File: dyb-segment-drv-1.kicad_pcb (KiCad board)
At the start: 2 copper layers, 76 x 76 mm, 192 parts, among them J1 Conn_01x10, Q1 HL2300, Q10 HL2300, Q11 HL2300, Q12 HL2300, Q13 HL2300, Q14 HL2300, Q15 HL2300, Q16 HL2300, Q2 HL2300, Q3 HL2300, Q4 HL2300, Q5 HL2300, Q6 HL2300, Q7 HL2300, Q8 HL2300, Q9 HL2300, SW1 SW_SPDT, U1 AP2112K-1.8, U10 74AUC2G32, U11 74AUC2G32, U12 74AUC2G32, U13 74AUC2G32, U14 74AUC2G32, U15 Inverter_Schmitt_Dual, U16 Inverter_Schmitt_Dual, U17 SN74AUP2G08, U18 SN74AUP2G08, U19 SN74AUP2G08, U2 GS3911AG, U20 SN74AUP2G08, U21 SN74AUP2G08, U22 74AUC2G32, U23 74AUC2G32, U24 74AUC2G32, U25 74AUC2G32, U26 74AUC2G32, U27 GS3911AG, U28 SN74AUP2G08, U29 SN74AUP2G08, U3 SN74AUP2G08, U30 SN74AUP2G08, U31 SN74AUP2G08, U32 SN74AUP2G08, U33 SN74AUP2G08, U34 74AUC2G32, U35 74AUC2G32, U36 74AUC2G32, U37 74AUC2G32, U38 74AUC2G32, U39 74AUC2G32, U4 SN74AUP2G08, U40 Inverter_Schmitt_Dual, U41 Inverter_Schmitt_Dual, U42 SN74AUP2G08, U43 SN74AUP2G08, U44 SN74AUP2G08, U45 SN74AUP2G08, U46 SN74AUP2G08, U47 74AUC2G32, U48 74AUC2G32, U49 74AUC2G32, U5 SN74AUP2G08, U50 74AUC2G32, U51 74AUC2G32, U6 SN74AUP2G08, U7 SN74AUP2G08, U8 SN74AUP2G08, U9 74AUC2G32

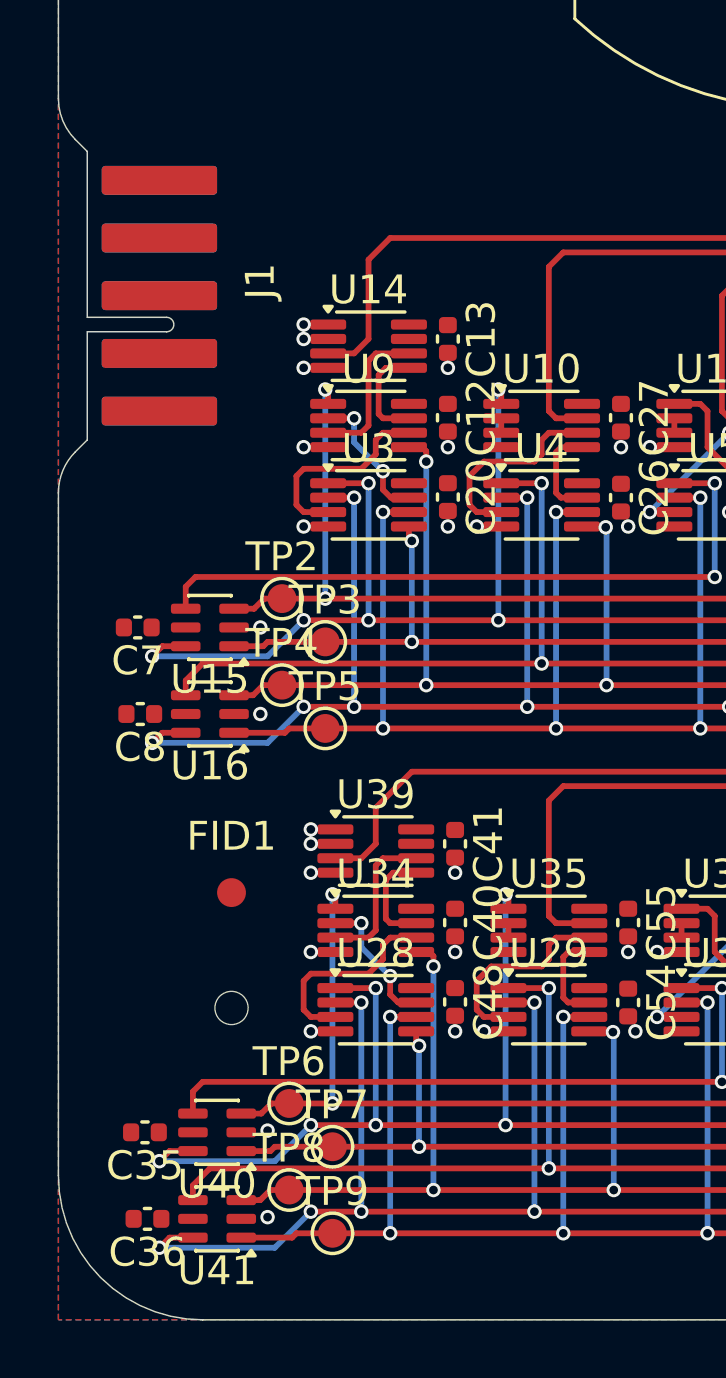
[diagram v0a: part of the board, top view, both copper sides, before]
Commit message: pcb: route gates inputs
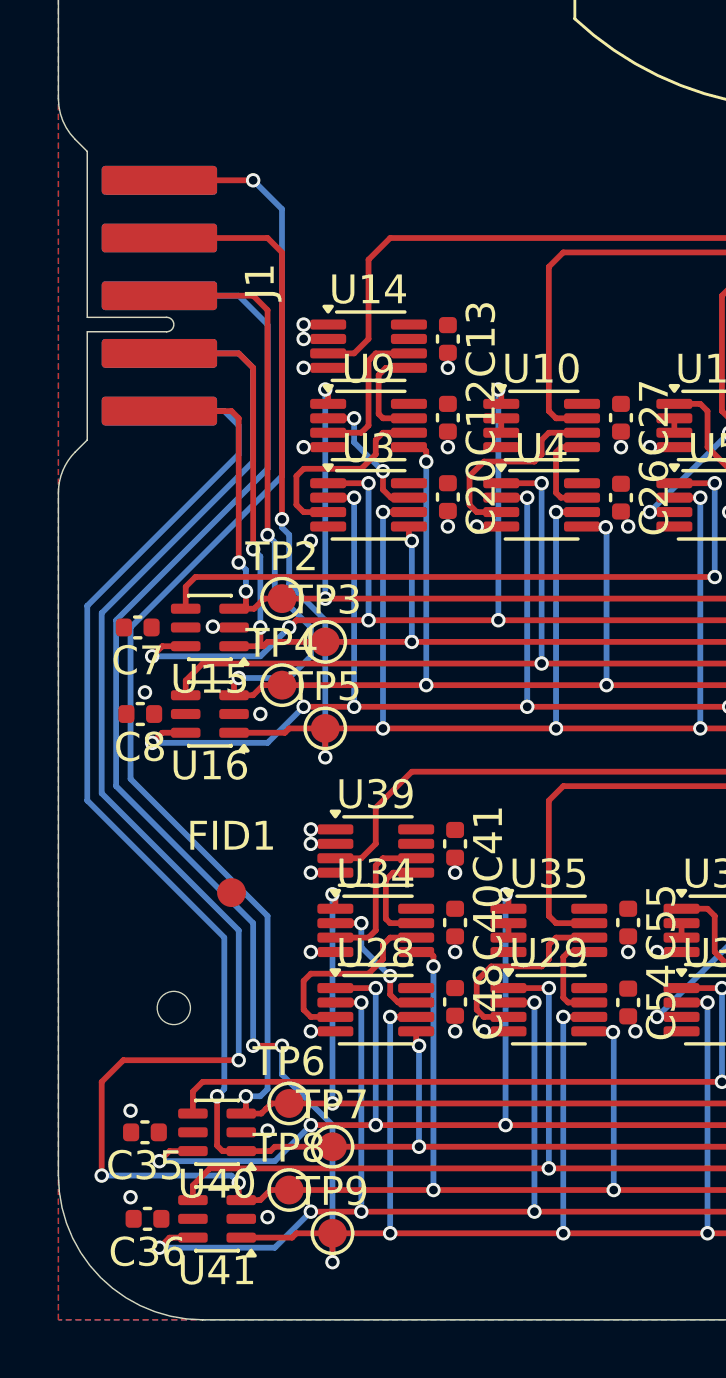
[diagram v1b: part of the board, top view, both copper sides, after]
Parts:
- moved H1 2.00 mm to (114.0, 84.2)
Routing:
- net /B2: track 108.0 -> 153.4 mm, vias 14 -> 17
- net /B3: track 61.0 -> 104.6 mm, vias 8 -> 11
- net /B0: track 72.8 -> 113.6 mm, vias 6 -> 8
- net /B1: track 91.7 -> 124.8 mm, vias 12 -> 13
- net /A3: track 61.0 -> 84.6 mm, vias 8 -> 10
- net /A2: track 108.0 -> 128.0 mm, vias 14 -> 16
- net /A1: track 91.8 -> 105.1 mm, vias 12 -> 14
- net /A0: track 72.8 -> 82.7 mm, vias 6 -> 8
- net GND: vias 143 -> 146

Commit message: pcb: route tvs diodes
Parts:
- added D10: H3V3L10B, GLCS:Diode_DFN1006, F.Cu at (112.5, 85.5)
- added D11: H3V3L10B, GLCS:Diode_DFN1006, F.Cu at (117.5, 92.5)
- added D4: H3V3L10B, GLCS:Diode_DFN1006, F.Cu at (115.7, 65.2)
- added D5: H3V3L10B, GLCS:Diode_DFN1006, F.Cu at (116.5, 61.1)
- added D6: H3V3L10B, GLCS:Diode_DFN1006, F.Cu at (116.5, 59.1)
- added D7: H3V3L10B, GLCS:Diode_DFN1006, F.Cu at (116.5, 56.9)
- added D8: H3V3L10B, GLCS:Diode_DFN1006, F.Cu at (114.0, 77.0)
- added D9: H3V3L10B, GLCS:Diode_DFN1006, F.Cu at (115.2, 82.8)
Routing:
- net GND: track 0.50 -> 3.62 mm, vias 146 -> 153
- net /B0: track 113.6 -> 114.0 mm, vias 8 -> 10
- net /B1: vias 13 -> 15

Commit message: pcb: route missing segments
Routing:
- net /Display/A: track 69.0 -> 80.8 mm, vias 0 -> 2
- net /Display/F: track 48.3 -> 57.7 mm, vias 2 -> 4
- net /Display/B: track 62.9 -> 70.6 mm, vias 0 -> 2
- net /Display/G: track 58.8 -> 65.7 mm
- net Net-(U27-A): track 0.00 -> 2.45 mm
- net Net-(U2-A): track 0.00 -> 2.45 mm
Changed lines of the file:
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@@
 	)
 	(segment
+		(start 163 23.74)
+		(end 163.01 23.75)
+		(width 0.2)
+		(layer "F.Cu")
+		(net "/Display/A")
+	)
+	(segment
+		(start 163 22.75)
+		(end 163 23.74)
+		(width 0.2)
+		(layer "F.Cu")
+		(net "/Display/A")
+	)
+	(segment
 		(start 120.25 61.5)
 		(end 120.75 61)
@@
 	)
 	(segment
+		(start 152.25 22.75)
+		(end 153.5 22.75)
+		(width 0.2)
+		(layer "F.Cu")
+		(net "/Display/A")
+	)
+	(segment
 		(start 119.35 61.5)
 		(end 120.25 61.5)
@@
 		(net "/Display/A")
 	)
+	(via
+		(at 163 22.75)
+		(size 0.5)
+		(drill 0.3)
+		(layers "F.Cu" "B.Cu")
+		(net "/Display/A")
+	)
+	(via
+		(at 153.5 22.75)
+		(size 0.5)
+		(drill 0.3)
+		(layers "F.Cu" "B.Cu")
+		(net "/Display/A")
+	)
+	(segment
+		(start 153.5 22.75)
+		(end 163 22.75)
+		(width 0.2)
+		(layer "B.Cu")
+		(net "/Display/A")
+	)
 	(segment
 		(start 114.4125 69.5875)
@@
 	)
 	(segment
+		(start 153.25 28.75)
+		(end 154 28)
+		(width 0.2)
+		(layer "F.Cu")
+		(net "/Display/G")
+	)
+	(segment
+		(start 154.18 23.82)
+		(end 154.74 23.82)
+		(width 0.2)
+		(layer "F.Cu")
+		(net "/Display/G")
+	)
+	(segment
+		(start 152.25 28.75)
+		(end 153.25 28.75)
+		(width 0.2)
+		(layer "F.Cu")
+		(net "/Display/G")
+	)
+	(segment
 		(start 150.5 49.2)
 		(end 150.55 49.25)
@@
 	)
 	(segment
+		(start 154 24)
+		(end 154.18 23.82)
+		(width 0.2)
+		(layer "F.Cu")
+		(net "/Display/G")
+	)
+	(segment
 		(start 156.45 57.45)
 		(end 159.5 60.5)
@@
 	)
 	(segment
+		(start 154 28)
+		(end 154 24)
+		(width 0.2)
+		(layer "F.Cu")
+		(net "/Display/G")
+	)
+	(segment
 		(start 150.5 29.5)
 		(end 150.5 49.2)
@@
 	)
 	(segment
+		(start 159.74 24.25)
+		(end 159.75 24.26)
+		(width 0.2)
+		(layer "F.Cu")
+		(net "/Display/B")
+	)
+	(segment
+		(start 152.25 24.75)
+		(end 153.5 24.75)
+		(width 0.2)
+		(layer "F.Cu")
+		(net "/Display/B")
+	)
+	(segment
 		(start 149.5 55.25)
 		(end 149.5 25.5)
@@
 	)
 	(segment
+		(start 158.75 24.25)
+		(end 159.74 24.25)
+		(width 0.2)
+		(layer "F.Cu")
+		(net "/Display/B")
+	)
+	(segment
 		(start 149.5 25.5)
 		(end 150.25 24.75)
@@
 		(net "/Display/B")
 	)
+	(via
+		(at 153.5 24.75)
+		(size 0.5)
+		(drill 0.3)
+		(layers "F.Cu" "B.Cu")
+		(net "/Display/B")
+	)
+	(via
+		(at 158.75 24.25)
+		(size 0.5)
+		(drill 0.3)
+		(layers "F.Cu" "B.Cu")
+		(net "/Display/B")
+	)
+	(segment
+		(start 153.5 24.75)
+		(end 158.25 24.75)
+		(width 0.2)
+		(layer "B.Cu")
+		(net "/Display/B")
+	)
+	(segment
+		(start 158.25 24.75)
+		(end 158.75 24.25)
+		(width 0.2)
+		(layer "B.Cu")
+		(net "/Display/B")
+	)
 	(segment
 		(start 154.74 46.21)
@@
 	)
 	(segment
+		(start 160.168037 28.74732)
+		(end 160.168037 30.518037)
+		(width 0.2)
+		(layer "F.Cu")
+		(net "Net-(U2-A)")
+	)
+	(segment
+		(start 160.168037 30.518037)
+		(end 160.65 31)
+		(width 0.2)
+		(layer "F.Cu")
+		(net "Net-(U2-A)")
+	)
+	(segment
 		(start 156.323139 28.745109)
 		(end 156.323139 30.473139)
@@
 	)
 	(segment
+		(start 152.25 26.75)
+		(end 153.5 26.75)
+		(width 0.2)
+		(layer "F.Cu")
+		(net "/Display/F")
+	)
+	(segment
 		(start 160.5 64.25)
 		(end 160.25 64)
@@
 	)
 	(segment
+		(start 160 25.25)
+		(end 159.26 25.25)
+		(width 0.2)
+		(layer "F.Cu")
+		(net "/Display/F")
+	)
+	(segment
 		(start 156.25 58)
 		(end 150 58)
@@
 	)
 	(via
+		(at 160 25.25)
+		(size 0.5)
+		(drill 0.3)
+		(layers "F.Cu" "B.Cu")
+		(net "/Display/F")
+	)
+	(via
 		(at 150 58)
 		(size 0.5)
@@
 		(net "/Display/F")
 	)
+	(via
+		(at 153.5 26.75)
+		(size 0.5)
+		(drill 0.3)
+		(layers "F.Cu" "B.Cu")
+		(net "/Display/F")
+	)
 	(segment
 		(start 150 50.05)
@@
 	)
 	(segment
+		(start 154.5 25.25)
+		(end 160 25.25)
+		(width 0.2)
+		(layer "B.Cu")
+		(net "/Display/F")
+	)
+	(segment
 		(start 150 58)
 		(end 150 50.05)
@@
 	)
 	(segment
+		(start 153.5 26.25)
+		(end 154.5 25.25)
+		(width 0.2)
+		(layer "B.Cu")
+		(net "/Display/F")
+	)
+	(segment
+		(start 153.5 26.75)
+		(end 153.5 26.25)
+		(width 0.2)
+		(layer "B.Cu")
+		(net "/Display/F")
+	)
+	(segment
 		(start 160.8 53.19)
 		(end 160.75 53.24)
@@
 	)
 	(segment
+		(start 170.168037 28.74732)
+		(end 170.168037 30.518037)
+		(width 0.2)
+		(layer "F.Cu")
+		(net "Net-(U27-A)")
+	)
+	(segment
+		(start 170.168037 30.518037)
+		(end 170.65 31)
+		(width 0.2)
+		(layer "F.Cu")
+		(net "Net-(U27-A)")
+	)
+	(segment

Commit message: pcb: add +1v8 routing
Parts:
- moved D4 0.83 mm to (116.5, 65.2)
- moved C10 0.27 mm to (141.5, 61.2)
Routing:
- net +1V8: track 4.38 -> 479.3 mm, vias 0 -> 32
- net /A2: track 128.0 -> 132.3 mm
- net /B1: track 124.8 -> 120.9 mm
- net /Display/E: track 15.8 -> 19.1 mm
- net /A1: track 105.2 -> 107.8 mm, vias 14 -> 15
- net /B0: track 114.0 -> 116.1 mm, vias 10 -> 12
- net /Display/G: track 65.7 -> 64.2 mm
- net /B2: track 153.5 -> 154.8 mm
- net /Display/A: track 80.8 -> 82.0 mm
- net /A0: track 82.7 -> 83.9 mm
- net GND: track 3.62 -> 2.56 mm
- net /B3: track 104.6 -> 105.4 mm
- net /Segment Driver/~{D3}: track 133.3 -> 132.8 mm
- net /Segment Driver/~{D1}: track 91.8 -> 91.3 mm

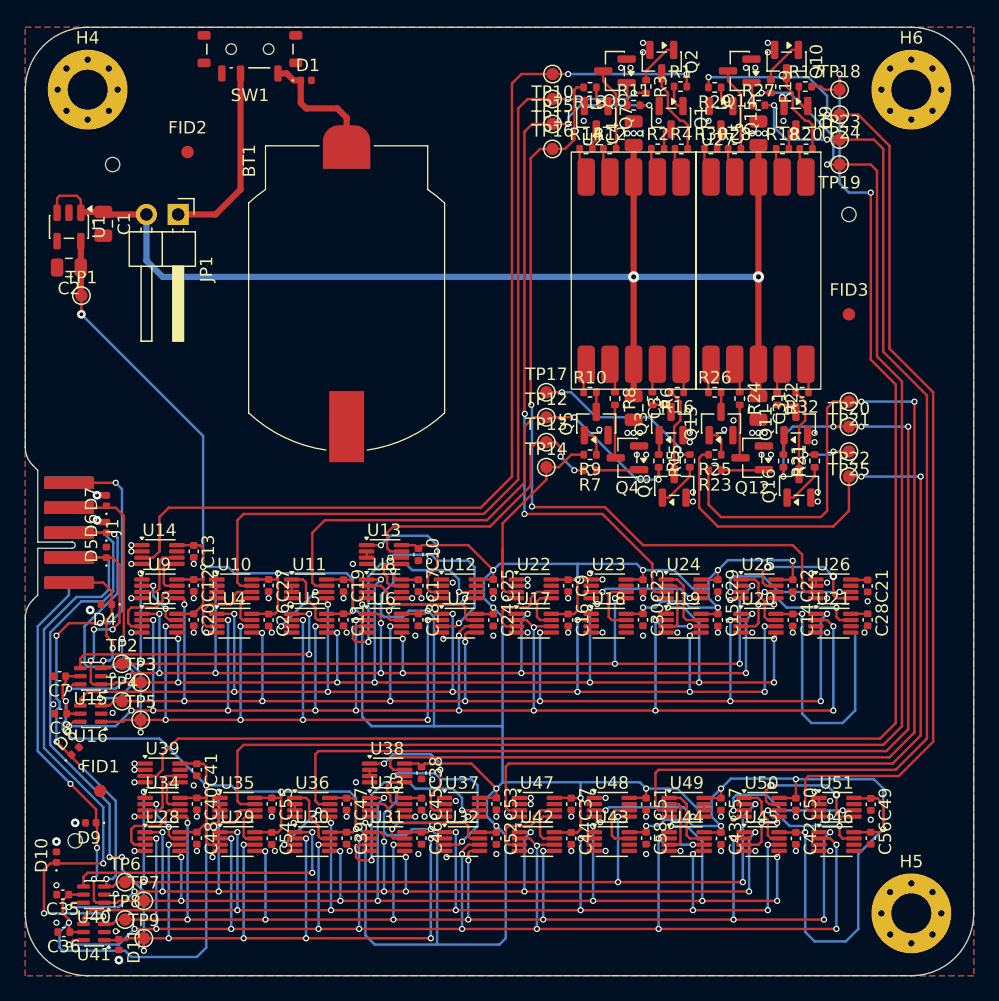
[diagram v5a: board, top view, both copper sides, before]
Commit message: pcb: add stitching vias
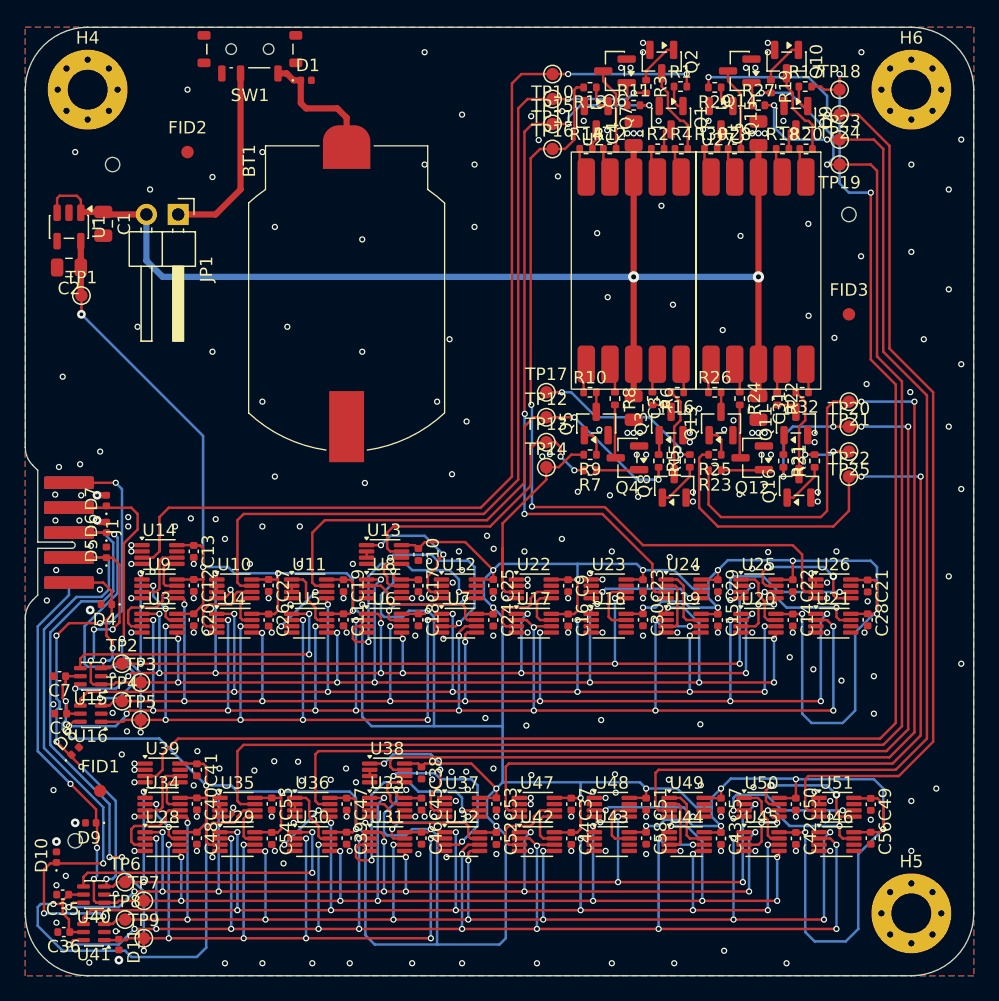
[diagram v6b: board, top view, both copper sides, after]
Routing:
- net +1V8: track 479.3 -> 500.7 mm, vias 32 -> 33
- net GND: track 2.56 -> 7.08 mm, vias 153 -> 299
- net /A3: track 84.7 -> 86.4 mm
- net /Segment Driver/~{D1}: track 91.3 -> 90.3 mm
